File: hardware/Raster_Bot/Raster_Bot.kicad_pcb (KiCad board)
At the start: 2 copper layers, 66 x 36 mm, 37 parts, among them J1 JUMPER_2PIN, J2 JUMPER_2PIN, J3 JUMPER_2PIN, J4 Conn_EYESPI, J5 Conn_Motor_N20_Encoder, J6 JST_PH, J7 PinSocket_1x02, J8 Conn_Motor_N20_Encoder, SW1 SW_SPDT, U1 DRV8833PWPR, U2 TPS61023DRLR

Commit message: Refactor filenames to Raster_Bot
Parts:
- J4: footprint raster-bot:XUNPU_FPC-05F-18PH20_1x18-1MP_P0.5mm_Horizontal -> Raster_Bot:XUNPU_FPC-05F-18PH20_1x18-1MP_P0.5mm_Horizontal
- SW1: footprint raster-bot:SW_SPDT_Shouhan_MSK12C02 -> Raster_Bot:SW_SPDT_Shouhan_MSK12C02
- U1: footprint raster-bot:HTSSOP-16-1EP_4.4x5mm_P0.65mm_EP3.4x5mm_Mask2.66x2.46mm_ThermalVias -> Raster_Bot:HTSSOP-16-1EP_4.4x5mm_P0.65mm_EP3.4x5mm_Mask2.66x2.46mm_ThermalVias
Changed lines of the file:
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@@
 		(property ki_fp_filters "R_*")
 		(sheetname "/")
-		(sheetfile "raster-bot.kicad_sch")
+		(sheetfile "Raster_Bot.kicad_sch")
 		(attr smd)
 		(fp_line
@@
 		(property ki_fp_filters "C_*")
 		(sheetname "/")
-		(sheetfile "raster-bot.kicad_sch")
+		(sheetfile "Raster_Bot.kicad_sch")
 		(attr smd)
 		(fp_line
@@
 		(property ki_fp_filters "Connector*:*_1x??_*")
 		(sheetname "/")
-		(sheetfile "raster-bot.kicad_sch")
+		(sheetfile "Raster_Bot.kicad_sch")
 		(attr through_hole)
 		(fp_line
@@
 		(property ki_fp_filters "Choke_* *Coil* Inductor_* L_*")
 		(sheetname "/")
-		(sheetfile "raster-bot.kicad_sch")
+		(sheetfile "Raster_Bot.kicad_sch")
 		(attr smd)
 		(fp_line
@@
 		(property ki_fp_filters "Arduino*Nano*")
 		(sheetname "/")
-		(sheetfile "raster-bot.kicad_sch")
+		(sheetfile "Raster_Bot.kicad_sch")
 		(attr through_hole exclude_from_bom)
 		(fp_line
@@
 		(property ki_fp_filters "C_*")
 		(sheetname "/")
-		(sheetfile "raster-bot.kicad_sch")
+		(sheetfile "Raster_Bot.kicad_sch")
 		(attr smd)
 		(fp_line
@@
 		(property ki_fp_filters "C_*")
 		(sheetname "/")
-		(sheetfile "raster-bot.kicad_sch")
+		(sheetfile "Raster_Bot.kicad_sch")
 		(attr smd)
 		(fp_line
@@
 		(property ki_fp_filters "MountingHole*")
 		(sheetname "/")
-		(sheetfile "raster-bot.kicad_sch")
+		(sheetfile "Raster_Bot.kicad_sch")
 		(attr exclude_from_pos_files exclude_from_bom)
 		(fp_circle
@@
 		(property ki_fp_filters "Pin* Test*")
 		(sheetname "/")
-		(sheetfile "raster-bot.kicad_sch")
+		(sheetfile "Raster_Bot.kicad_sch")
 		(attr exclude_from_pos_files exclude_from_bom)
 		(fp_line
@@
 		(property ki_fp_filters "LED* LED_SMD:* LED_THT:*")
 		(sheetname "/")
-		(sheetfile "raster-bot.kicad_sch")
+		(sheetfile "Raster_Bot.kicad_sch")
 		(attr smd)
 		(fp_line
@@
 		(property ki_fp_filters "Pin* Test*")
 		(sheetname "/")
-		(sheetfile "raster-bot.kicad_sch")
+		(sheetfile "Raster_Bot.kicad_sch")
 		(attr exclude_from_pos_files exclude_from_bom)
 		(fp_line
@@
 		(property ki_fp_filters "C_*")
 		(sheetname "/")
-		(sheetfile "raster-bot.kicad_sch")
+		(sheetfile "Raster_Bot.kicad_sch")
 		(attr smd)
 		(fp_line
@@
 		(property ki_fp_filters "LED* LED_SMD:* LED_THT:*")
 		(sheetname "/")
-		(sheetfile "raster-bot.kicad_sch")
+		(sheetfile "Raster_Bot.kicad_sch")
 		(attr smd)
 		(fp_line
@@
 		(property ki_fp_filters "R_*")
 		(sheetname "/")
-		(sheetfile "raster-bot.kicad_sch")
+		(sheetfile "Raster_Bot.kicad_sch")
 		(attr smd)
 		(fp_line
@@
 		)
 		(sheetname "/")
-		(sheetfile "raster-bot.kicad_sch")
+		(sheetfile "Raster_Bot.kicad_sch")
 		(attr smd)
 		(fp_line
@@
 		(property ki_fp_filters "Connector*:*_1x??_*")
 		(sheetname "/")
-		(sheetfile "raster-bot.kicad_sch")
+		(sheetfile "Raster_Bot.kicad_sch")
 		(attr through_hole exclude_from_bom)
 		(fp_line
@@
 		(property ki_fp_filters "Connector*:*_1x??_*")
 		(sheetname "/")
-		(sheetfile "raster-bot.kicad_sch")
+		(sheetfile "Raster_Bot.kicad_sch")
 		(attr through_hole)
 		(fp_line
@@
 		)
 	)
-	(footprint "raster-bot:SW_SPDT_Shouhan_MSK12C02"
+	(footprint "Raster_Bot:SW_SPDT_Shouhan_MSK12C02"
 		(layer "F.Cu")
 		(at 130.2372 77.3954 180)
@@
 		)
 		(sheetname "/")
-		(sheetfile "raster-bot.kicad_sch")
+		(sheetfile "Raster_Bot.kicad_sch")
 		(attr smd)
 		(fp_line
@@
 		(property ki_fp_filters "Connector*:*_1x??_*")
 		(sheetname "/")
-		(sheetfile "raster-bot.kicad_sch")
+		(sheetfile "Raster_Bot.kicad_sch")
 		(attr through_hole)
 		(fp_line
@@
 		(property ki_fp_filters "R_*")
 		(sheetname "/")
-		(sheetfile "raster-bot.kicad_sch")
+		(sheetfile "Raster_Bot.kicad_sch")
 		(attr smd)
 		(fp_line
@@
 		(property ki_fp_filters "R_*")
 		(sheetname "/")
-		(sheetfile "raster-bot.kicad_sch")
+		(sheetfile "Raster_Bot.kicad_sch")
 		(attr smd)
 		(fp_line
@@
 		)
 	)
-	(footprint "raster-bot:XUNPU_FPC-05F-18PH20_1x18-1MP_P0.5mm_Horizontal"
+	(footprint "Raster_Bot:XUNPU_FPC-05F-18PH20_1x18-1MP_P0.5mm_Horizontal"
 		(layer "F.Cu")
 		(at 131.3 105.1)
@@
 		)
 		(sheetname "/")
-		(sheetfile "raster-bot.kicad_sch")
+		(sheetfile "Raster_Bot.kicad_sch")
 		(attr smd)
 		(fp_line
@@
 		)
 		(sheetname "/")
-		(sheetfile "raster-bot.kicad_sch")
+		(sheetfile "Raster_Bot.kicad_sch")
 		(attr smd)
 		(fp_line
@@
 		(property ki_fp_filters "Pin* Test*")
 		(sheetname "/")
-		(sheetfile "raster-bot.kicad_sch")
+		(sheetfile "Raster_Bot.kicad_sch")
 		(attr exclude_from_pos_files exclude_from_bom)
 		(fp_line
@@
 		(property ki_fp_filters "C_*")
 		(sheetname "/")
-		(sheetfile "raster-bot.kicad_sch")
+		(sheetfile "Raster_Bot.kicad_sch")
 		(attr smd)
 		(fp_line
@@
 		(property ki_fp_filters "MountingHole*")
 		(sheetname "/")
-		(sheetfile "raster-bot.kicad_sch")
+		(sheetfile "Raster_Bot.kicad_sch")
 		(attr exclude_from_pos_files exclude_from_bom)
 		(fp_circle
@@
 		(property ki_fp_filters "Connector*:*_1x??_*")
 		(sheetname "/")
-		(sheetfile "raster-bot.kicad_sch")
+		(sheetfile "Raster_Bot.kicad_sch")
 		(attr through_hole)
 		(fp_line
@@
 		(property ki_fp_filters "C_*")
 		(sheetname "/")
-		(sheetfile "raster-bot.kicad_sch")
+		(sheetfile "Raster_Bot.kicad_sch")
 		(attr smd)
 		(fp_line
@@
 		)
 	)
-	(footprint "raster-bot:HTSSOP-16-1EP_4.4x5mm_P0.65mm_EP3.4x5mm_Mask2.66x2.46mm_ThermalVias"
+	(footprint "Raster_Bot:HTSSOP-16-1EP_4.4x5mm_P0.65mm_EP3.4x5mm_Mask2.66x2.46mm_ThermalVias"
 		(layer "F.Cu")
 		(at 166.8932 96.2104 90)
@@
 		(property ki_fp_filters "HTSSOP*1EP*4.4x5mm*P0.65mm*EP3.4x5mm*")
 		(sheetname "/")
-		(sheetfile "raster-bot.kicad_sch")
+		(sheetfile "Raster_Bot.kicad_sch")
 		(attr smd)
 		(fp_line
@@
 		(property ki_fp_filters "MountingHole*")
 		(sheetname "/")
-		(sheetfile "raster-bot.kicad_sch")
+		(sheetfile "Raster_Bot.kicad_sch")
 		(attr exclude_from_pos_files exclude_from_bom)
 		(fp_circle
@@
 		(property ki_fp_filters "R_*")
 		(sheetname "/")
-		(sheetfile "raster-bot.kicad_sch")
+		(sheetfile "Raster_Bot.kicad_sch")
 		(attr smd)
 		(fp_line
@@
 		(property ki_fp_filters "C_*")
 		(sheetname "/")
-		(sheetfile "raster-bot.kicad_sch")
+		(sheetfile "Raster_Bot.kicad_sch")
 		(attr smd)
 		(fp_line
@@
 		(property ki_fp_filters "C_*")
 		(sheetname "/")
-		(sheetfile "raster-bot.kicad_sch")
+		(sheetfile "Raster_Bot.kicad_sch")
 		(attr smd)
 		(fp_line
@@
 		(property ki_fp_filters "Pin* Test*")
 		(sheetname "/")
-		(sheetfile "raster-bot.kicad_sch")
+		(sheetfile "Raster_Bot.kicad_sch")
 		(attr exclude_from_pos_files exclude_from_bom)
 		(fp_line
@@
 		(property ki_fp_filters "MountingHole*")
 		(sheetname "/")
-		(sheetfile "raster-bot.kicad_sch")
+		(sheetfile "Raster_Bot.kicad_sch")
 		(attr exclude_from_pos_files exclude_from_bom)
 		(fp_circle
@@
 		)
 		(sheetname "/")
-		(sheetfile "raster-bot.kicad_sch")
+		(sheetfile "Raster_Bot.kicad_sch")
 		(attr smd)
 		(fp_line
@@
 		(property ki_fp_filters "R_*")
 		(sheetname "/")
-		(sheetfile "raster-bot.kicad_sch")
+		(sheetfile "Raster_Bot.kicad_sch")
 		(attr smd)
 		(fp_line

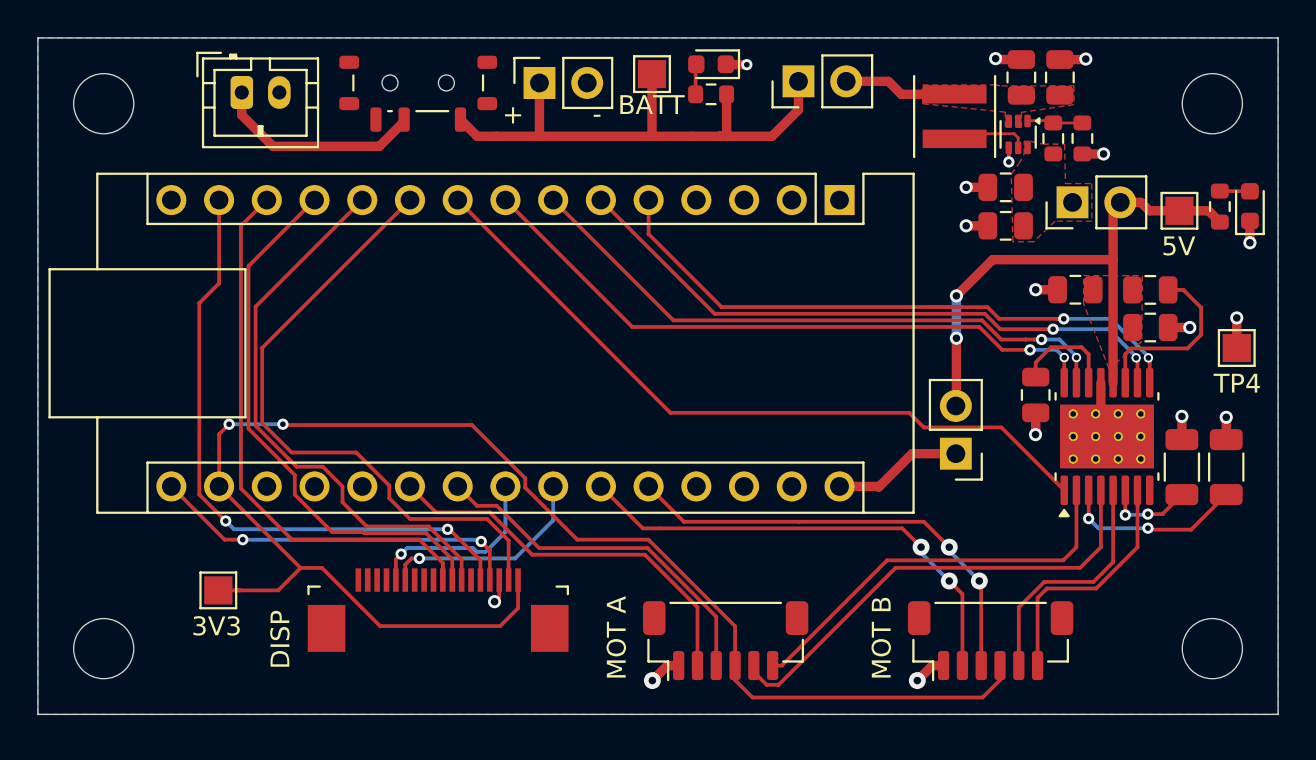
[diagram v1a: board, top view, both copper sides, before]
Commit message: [hardware] v0.3 - design upgrade featuring esp32-s3, battery charger, 3.3V LDO, 5V boost coverter
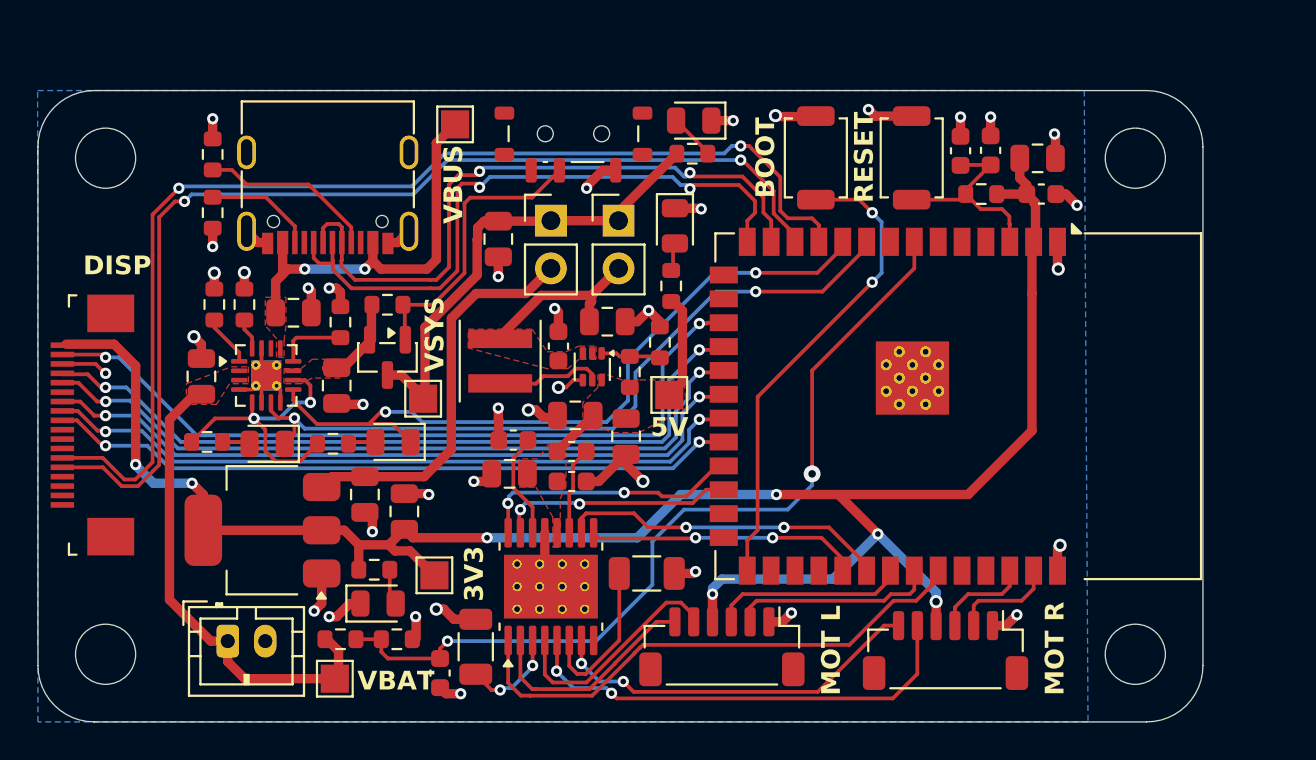
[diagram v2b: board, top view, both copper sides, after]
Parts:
- removed A1: Arduino_Nano_ESP32, Module:Arduino_Nano
- removed J7: PinSocket_1x02, Connector_PinSocket_2.54mm:PinSocket_1x02_P2.54mm_Vertical
- added C10: 0.1uF, Capacitor_SMD:C_0603_1608Metric, F.Cu at (138.4, 98.6)
- added C11: 10uF, Capacitor_SMD:C_0805_2012Metric, F.Cu at (135.1, 98.2)
- added C12: 10uF, Capacitor_SMD:C_0805_2012Metric, F.Cu at (127.4, 99.3)
- added C13: 22uF, Capacitor_SMD:C_0805_2012Metric, F.Cu at (129.5, 100.2)
- added C14: 1uF, Capacitor_SMD:C_0603_1608Metric, F.Cu at (131.4, 108.8)
- added C15: 22uF, Capacitor_SMD:C_0805_2012Metric, F.Cu at (138.6, 95.1)
- added C16: 22uF, Capacitor_SMD:C_0805_2012Metric, F.Cu at (141.3, 96.2)
- added C17: 0.1uF, Capacitor_SMD:C_0603_1608Metric, F.Cu at (137.7, 91.4)
- added C18: 10uF, Capacitor_SMD:C_0805_2012Metric, F.Cu at (140.3, 90.1)
- added C19: 22uF, Capacitor_SMD:C_0805_2012Metric, F.Cu at (134.5, 85.7)
- added C9: 0.01uF, Capacitor_SMD:C_0603_1608Metric, F.Cu at (138.4, 97.0)
- added D3: LED, LED_SMD:LED_0805_2012Metric, F.Cu at (144.9, 79.4)
- added D4: LED, LED_SMD:LED_0805_2012Metric, F.Cu at (143.9, 85.0)
- added D5: LED, LED_SMD:LED_0805_2012Metric, F.Cu at (128.1, 105.1)
- added Q1: AO3401A, Package_TO_SOT_SMD:SOT-23, F.Cu at (128.6, 92.0)
- added R10: 2.2k, Resistor_SMD:R_0603_1608Metric, F.Cu at (143.7, 88.2)
- added R11: 2.2k, Resistor_SMD:R_0603_1608Metric, F.Cu at (127.9, 103.3)
- added R12: 0.2, Resistor_SMD:R_1206_3216Metric, F.Cu at (133.3, 107.4)
- added R13: 0.2, Resistor_SMD:R_1206_3216Metric, F.Cu at (142.4, 103.5)
- added R14: 200k, Resistor_SMD:R_0603_1608Metric, F.Cu at (126.1, 107.0)
- added R15: 200k, Resistor_SMD:R_0603_1608Metric, F.Cu at (129.1, 107.0)
- added R16: 100k, Resistor_SMD:R_0603_1608Metric, F.Cu at (128.6, 89.2)
- added R17: 220k, Resistor_SMD:R_0603_1608Metric, F.Cu at (141.5, 92.8)
- added R18: 30k, Resistor_SMD:R_0603_1608Metric, F.Cu at (143.1, 91.2)
- added R7: 2.2k, Resistor_SMD:R_0603_1608Metric, F.Cu at (125.7, 96.6)
- added R8: 10k, Resistor_SMD:R_0603_1608Metric, F.Cu at (160.2, 83.3)
- added R9: 2.2k, Resistor_SMD:R_0603_1608Metric, F.Cu at (144.8, 81.2)
- added SW2: SW_RESET, Button_Switch_SMD:SW_SPST_TS-1088-xR020, F.Cu at (156.5, 81.4)
- added SW3: SW_BOOT, Button_Switch_SMD:SW_SPST_TS-1088-xR020, F.Cu at (151.4, 81.4)
- added TP5: TestPoint, TestPoint:TestPoint_Pad_1.5x1.5mm, F.Cu at (143.6, 94.0)
- added U3: DRV8833PWPR, Raster_Bot:HTSSOP-16-1EP_4.4x5mm_P0.65mm_EP3.4x5mm_Mask2.66x2.46mm_ThermalVias, F.Cu at (137.3, 104.2)
- added U4: AP2114H-3.3, Package_TO_SOT_SMD:SOT-223-3_TabPin2, F.Cu at (122.0, 101.2)
- added U5: TPS61023DRLR, Package_TO_SOT_SMD:SOT-563, F.Cu at (139.5, 92.5)
- C1: value 2.2uF -> 10uF
- C2: value 0.01uF -> 10uF
- C3: value 0.1uF -> 10uF
- C4: value 10uF -> 1uF; footprint Capacitor_SMD:C_0805_2012Metric -> Capacitor_SMD:C_0603_1608Metric
- C5: footprint Capacitor_SMD:C_0805_2012Metric -> Capacitor_SMD:C_0603_1608Metric
- C6: value 10uF -> 22uF
- C7: value 22uF -> 0.1uF; footprint Capacitor_SMD:C_0805_2012Metric -> Capacitor_SMD:C_0603_1608Metric
- C8: value 22uF -> 2.2uF; footprint Capacitor_SMD:C_0805_2012Metric -> Capacitor_SMD:C_0603_1608Metric
- D1, D2: footprint LED_SMD:LED_0603_1608Metric -> LED_SMD:LED_0805_2012Metric
- J1: value JUMPER_2PIN -> JST_PH; footprint Connector_PinHeader_2.54mm:PinHeader_1x02_P2.54mm_Vertical -> Connector_JST:JST_PH_B2B-PH-K_1x02_P2.00mm_Vertical
- J2: value JUMPER_2PIN -> USB_C_Receptacle_USB2.0_16P; footprint Connector_PinHeader_2.54mm:PinHeader_1x02_P2.54mm_Vertical -> Raster_Bot:USB_C_Receptacle_G-Switch_GT-USB-7010ASV
- J3: value JUMPER_2PIN -> Conn_Motor_N20_Encoder; footprint Connector_PinHeader_2.54mm:PinHeader_1x02_P2.54mm_Vertical -> Connector_JST:JST_SH_BM06B-SRSS-TB_1x06-1MP_P1.00mm_Vertical
- J5, J8: value Conn_Motor_N20_Encoder -> JUMPER_2PIN; footprint Connector_JST:JST_SH_BM06B-SRSS-TB_1x06-1MP_P1.00mm_Vertical -> Connector_PinHeader_2.54mm:PinHeader_1x02_P2.54mm_Vertical
- J6: value JST_PH -> Conn_Motor_N20_Encoder; footprint Connector_JST:JST_PH_B2B-PH-K_1x02_P2.00mm_Vertical -> Connector_JST:JST_SH_BM06B-SRSS-TB_1x06-1MP_P1.00mm_Vertical
- R1, R2: value 0.2 -> 5.1k; footprint Resistor_SMD:R_1206_3216Metric -> Resistor_SMD:R_0603_1608Metric
- R3: value 220k -> 1.1k
- R4: value 30k -> 2.7k
- R5: value 2.2k -> 10k
- SW1: value SW_SPDT -> SW_SPDT_SH; footprint Raster_Bot:SW_SPDT_Shouhan_MSK12C02 -> Button_Switch_SMD:SW_SPDT_Shouhan_MSK12C02
- U1: value DRV8833PWPR -> BQ24072RGT; footprint Raster_Bot:HTSSOP-16-1EP_4.4x5mm_P0.65mm_EP3.4x5mm_Mask2.66x2.46mm_ThermalVias -> Package_DFN_QFN:VQFN-16-1EP_3x3mm_P0.5mm_EP1.6x1.6mm_ThermalVias
- U2: value TPS61023DRLR -> ESP32-S3-WROOM-1; footprint Package_TO_SOT_SMD:SOT-563 -> Raster_Bot:ESP32-S3-WROOM-1
- moved H2 65.8 mm to (113.6, 107.8)
- moved H3 60.8 mm to (168.4, 81.4)
- moved R1 55.6 mm to (119.3, 84.3), turned to -90 degrees
- moved R6 55.3 mm to (119.0, 96.5), turned to 0 degrees
- moved R2 54.2 mm to (119.3, 81.2)
- moved TP2 51.4 mm to (125.8, 109.1)
- moved C3 50.6 mm to (118.7, 93.0), turned to 90 degrees
- moved J6 47.8 mm to (158.3, 107.6), turned to 180 degrees
- moved D2 47.3 mm to (128.9, 96.5), turned to 180 degrees
- moved R4 45.5 mm to (121.0, 89.2), turned to 90 degrees
- moved U1 44.9 mm to (122.2, 93.0), turned to 0 degrees
- moved TP4 44.4 mm to (131.1, 103.6)
- moved C2 43.6 mm to (125.9, 93.5), turned to -90 degrees
- moved J1 40.0 mm to (120.1, 107.1), turned to 0 degrees
- moved C1 39.7 mm to (123.6, 89.6), turned to 180 degrees
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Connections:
- C1 pad 1: Net-(U1-VINT) -> GND
- C1 pad 2: GND -> VBUS
- C2 pad 1: +5V -> VSYS_SRC
- C2 pad 2: Net-(U1-VCP) -> GND
- C3 pad 1: +5V -> VBAT
- C4 pad 1: +5V -> /RESET
- C5 pad 1: +BATT -> +3V3
- C6 pad 1: +BATT -> +3V3
- C7 pad 1: +5V -> /RESET
- C8 pad 1: +5V -> Net-(U3-VINT)
- D1 pad 1: GND -> /PGOOD
- D2 pad 1: GND -> /CHG
- J1 pad 1: +5V -> VBAT
- J1 pad 2: +5V -> GND
- J3 pad 1: +BATT -> GND
- J3 pad 2: +BATT -> /MOT1_ENCB
- J4 pad 1: +3V3 -> unconnected-(J4-GPIO2-Pad1)
- J4 pad 10: unconnected-(J4-SD_CS-Pad10) -> /CS
- J4 pad 11: unconnected-(J4-MEM_CS-Pad11) -> /RST
- J4 pad 12: unconnected-(J4-TS_CS-Pad12) -> /DC
- J4 pad 13: /SCL -> unconnected-(J4-MISO-Pad13)
- J4 pad 14: /SDA -> /MOSI
- J4 pad 15: unconnected-(J4-INT-Pad15) -> /SCK
- J4 pad 16: unconnected-(J4-BUSY/TE-Pad16) -> GND
- J4 pad 17: unconnected-(J4-GPIO1-Pad17) -> /LITE
- J4 pad 18: unconnected-(J4-GPIO2-Pad18) -> +3V3
- J4 pad 2: /LITE -> unconnected-(J4-GPIO1-Pad2)
- J4 pad 3: GND -> unconnected-(J4-BUSY/TE-Pad3)
- J4 pad 4: /SCK -> unconnected-(J4-INT-Pad4)
- J4 pad 5: /MOSI -> /SDA
- J4 pad 6: unconnected-(J4-MISO-Pad6) -> /SCL
- J4 pad 7: /DC -> unconnected-(J4-TS_CS-Pad7)
- J4 pad 8: /RST -> unconnected-(J4-MEM_CS-Pad8)
- J4 pad 9: /CS -> unconnected-(J4-SD_CS-Pad9)
- J5 pad 1: GND -> VSYS
- J5 pad 2: /A_ENCB -> /VSYS_3VIN
- J6 pad 1: Net-(J6-Pin_1) -> GND
- J6 pad 2: GND -> /MOT2_ENCB
- J8 pad 1: GND -> VSYS
- J8 pad 2: /B_ENCB -> /VSYS_5VIN
- L1 pad 1: +BATT -> /VSYS_5VIN
- L1 pad 2: Net-(U2-SW) -> Net-(U5-SW)
- R1 pad 1: Net-(U1-AISEN) -> Net-(J2-CC2)
- R2 pad 1: Net-(U1-BISEN) -> Net-(J2-CC1)
- R3 pad 1: +5V -> Net-(U1-ILIM)
- R3 pad 2: Net-(U2-FB) -> GND
- R4 pad 1: Net-(U2-FB) -> Net-(U1-ISET)
- R5 pad 1: +BATT -> Net-(U1-TS)
- R5 pad 2: Net-(D1-A) -> GND
- R6 pad 1: +5V -> VSYS_SRC
- R6 pad 2: Net-(D2-A) -> Net-(D1-A)
- SW1 pad 1: +BATT -> GND
- SW1 pad 2: Net-(J6-Pin_1) -> Net-(Q1-G)
- TP1 pad 1: +3V3 -> VBUS
- TP2 pad 1: +5V -> VBAT
- TP3 pad 1: +BATT -> VSYS
- TP4 pad 1: GND -> +3V3
- U1 pad 1: /SLEEP -> Net-(U1-TS)
- U1 pad 10: /B_IN2 -> VSYS_SRC
- U1 pad 11: Net-(U1-VCP) -> VSYS_SRC
- U1 pad 12: +5V -> Net-(U1-ILIM)
- U1 pad 13: GND -> VBUS
- U1 pad 14: Net-(U1-VINT) -> unconnected-(U1-TMR-Pad14)
- U1 pad 15: /A_IN2 -> GND
- U1 pad 16: /A_IN1 -> Net-(U1-ISET)
- U1 pad 2: /A_OUT1 -> VBAT
- U1 pad 3: Net-(U1-AISEN) -> VBAT
- U1 pad 4: /A_OUT2 -> GND
- U1 pad 5: /B_OUT2 -> VSYS_SRC
- U1 pad 6: Net-(U1-BISEN) -> GND
- U1 pad 7: /B_OUT1 -> /PGOOD
- U1 pad 8: unconnected-(U1-~{FAULT}-Pad8) -> GND
- U1 pad 9: /B_IN1 -> /CHG
- U2 pad 1: Net-(U2-FB) -> GND
- U2 pad 2: +BATT -> +3V3
- U2 pad 3: +BATT -> /RESET
- U2 pad 4: GND -> unconnected-(U2-IO4-Pad4)
- U2 pad 5: Net-(U2-SW) -> unconnected-(U2-IO5-Pad5)
- U2 pad 6: +5V -> unconnected-(U2-IO6-Pad6)
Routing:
- net /SCL: track 11.5 -> 59.5 mm, vias 1 -> 2
- net GND: track 24.7 -> 71.2 mm, vias 17 -> 38
- net /SDA: track 10.6 -> 57.0 mm, vias 1 -> 2
- net /VBAT_DIV: track 0.00 -> 45.9 mm, vias 0 -> 2
- net /PGOOD: track 0.00 -> 39.5 mm, vias 0 -> 2
- net /CHG: track 0.00 -> 38.9 mm, vias 0 -> 2
- net /USB_D-: track 0.00 -> 35.2 mm, vias 0 -> 2
- net +BATT: track 34.8 -> 0.00 mm
- net /A_IN1: track 34.6 -> 0.00 mm, vias 2 -> 0
- net /USB_D+: track 0.00 -> 34.5 mm, vias 0 -> 2
- net /B_IN1: track 34.4 -> 0.00 mm, vias 2 -> 0
- net /B_IN2: track 33.5 -> 0.00 mm, vias 2 -> 0
- net /A_IN2: track 32.7 -> 0.00 mm, vias 2 -> 0
- net +5V: track 37.5 -> 8.19 mm, vias 2 -> 0
- net VBAT: track 0.00 -> 25.6 mm
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- added copper zone on F.Cu, net /VSYS_5VIN
- added copper zone on F.Cu, net VBAT
- added copper zone on F.Cu, net VBUS
- added copper zone on F.Cu, net VSYS_SRC
- removed copper zone on F.Cu, net +BATT
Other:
- board size 66 x 36 mm -> 62 x 33.6 mm
- board text added: "BOOT"
- board text added: "MOT L"
- board text added: "MOT R"
- board text added: "RESET"
- board text added: "VBAT"
- board text added: "VBUS"
- board text added: "VSYS"
- board text added: "no"
- board text added: "rx"
- board text added: "tx"
- board text removed: "+"
- board text removed: "-"
- board text removed: "BATT"
- board text removed: "MOT A"
- board text removed: "MOT B"
- board text removed: "Raster Bot ${REVISION}"

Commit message: [hardware] Add version silkscreen;
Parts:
- U1: footprint Package_DFN_QFN:VQFN-16-1EP_3x3mm_P0.5mm_EP1.6x1.6mm_ThermalVias -> Raster_Bot:VQFN-16-1EP_3x3mm_P0.5mm_EP1.6x1.6mm_ThermalVias
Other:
- board text added: "Raster Bot ${REVISION}"
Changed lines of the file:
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@@
 		)
 	)
-	(footprint "Package_DFN_QFN:VQFN-16-1EP_3x3mm_P0.5mm_EP1.6x1.6mm_ThermalVias"
+	(footprint "Raster_Bot:VQFN-16-1EP_3x3mm_P0.5mm_EP1.6x1.6mm_ThermalVias"
 		(layer "F.Cu")
 		(at 122.15 92.9625)
@@
 		)
 		(pad "17" thru_hole circle
-			(at -0.55 -0.55)
+			(at -0.4 -0.4)
 			(size 0.5 0.5)
-			(drill 0.2)
+			(drill 0.3)
 			(property pad_prop_heatsink)
 			(layers "*.Cu")
@@
 		)
 		(pad "17" thru_hole circle
-			(at -0.55 0.55)
+			(at -0.4 0.4)
 			(size 0.5 0.5)
-			(drill 0.2)
+			(drill 0.3)
 			(property pad_prop_heatsink)
 			(layers "*.Cu")
@@
 		)
 		(pad "17" thru_hole circle
-			(at 0.55 -0.55)
+			(at 0.4 -0.4)
 			(size 0.5 0.5)
-			(drill 0.2)
+			(drill 0.3)
 			(property pad_prop_heatsink)
 			(layers "*.Cu")
@@
 		)
 		(pad "17" thru_hole circle
-			(at 0.55 0.55)
+			(at 0.4 0.4)
 			(size 0.5 0.5)
-			(drill 0.2)
+			(drill 0.3)
 			(property pad_prop_heatsink)
 			(layers "*.Cu")
@@
 		)
 	)
+	(gr_text "Raster Bot\n${REVISION}"
+		(at 163.4 109.8 0)
+		(layer "B.SilkS")
+		(effects
+			(font
+				(size 2 2)
+				(thickness 0.3)
+			)
+			(justify left bottom mirror)
+		)
+	)
